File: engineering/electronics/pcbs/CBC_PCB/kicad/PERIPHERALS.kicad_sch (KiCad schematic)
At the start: 7 parts, among them J2 AT13-12PB-BM03

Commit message: electronics: integrate CBC PCB updates
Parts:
- C25, C26: symbol EasyEDA_Lib:CC0402KRX7R7BB104 -> CBC_PCB:CC0402KRX7R7BB104
- J2: symbol 2026-04-30_07-21-07:AT13-12PB-BM03 -> CBC_PCB:AT13-12PB-BM03
- R10, R11: symbol EasyEDA_Lib:RC0402FR-074K7L -> CBC_PCB:RC0402FR-074K7L
- U1, U6: symbol EasyEDA_Lib:DS18B20Z+T&amp;R -> CBC_PCB:DS18B20Z+T&amp;R

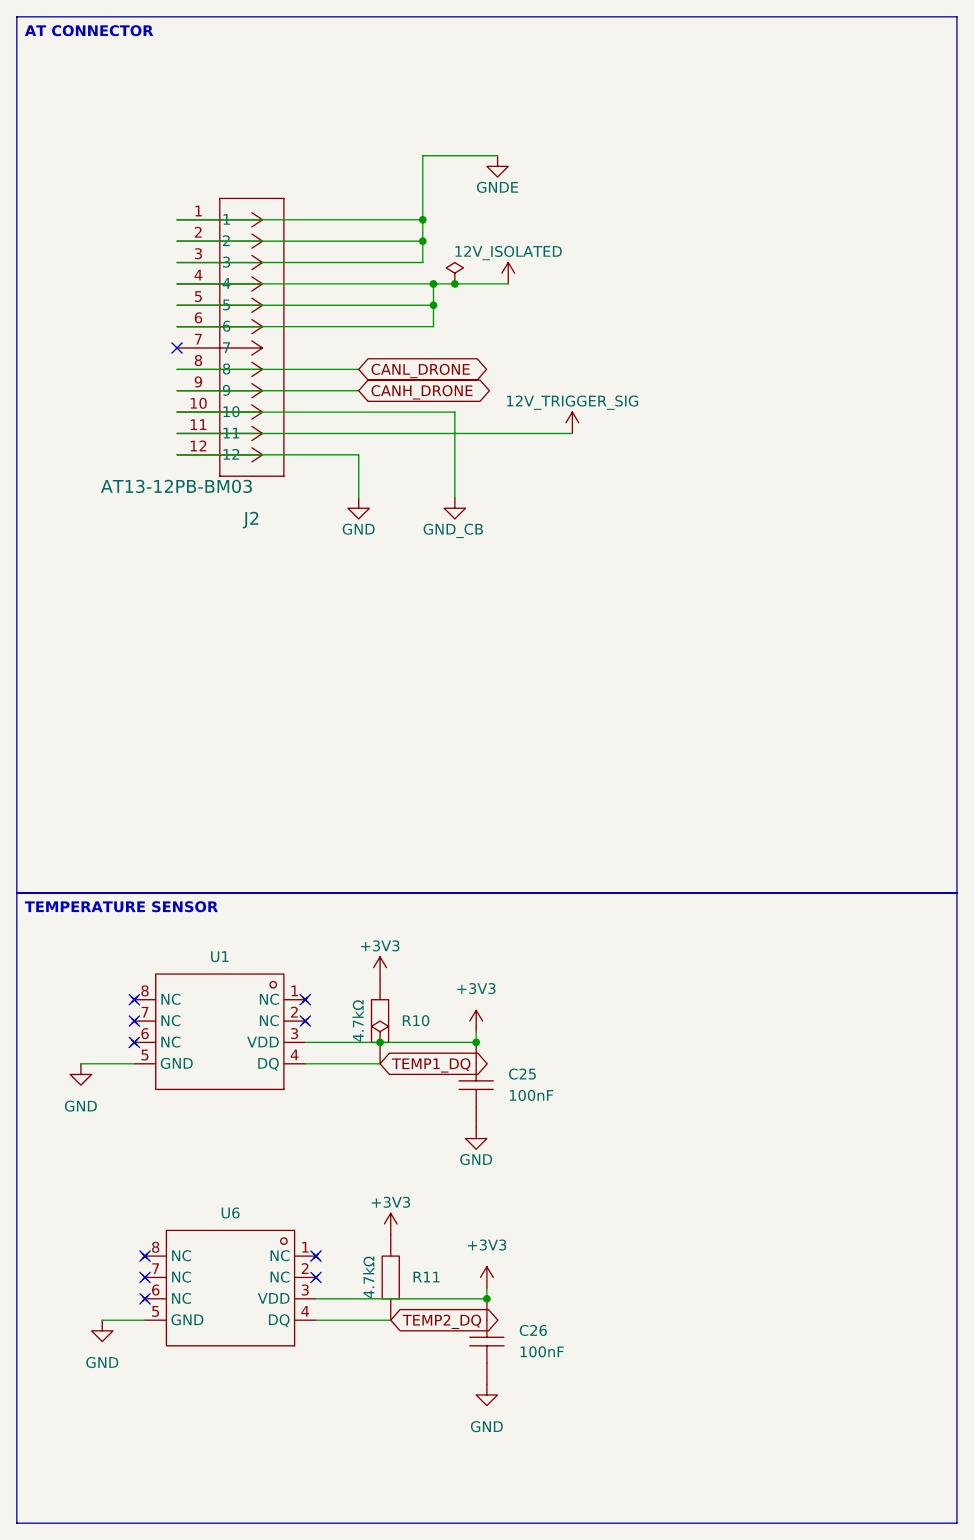
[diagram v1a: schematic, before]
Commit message: electronics: update CMAIN and CBC PCB files
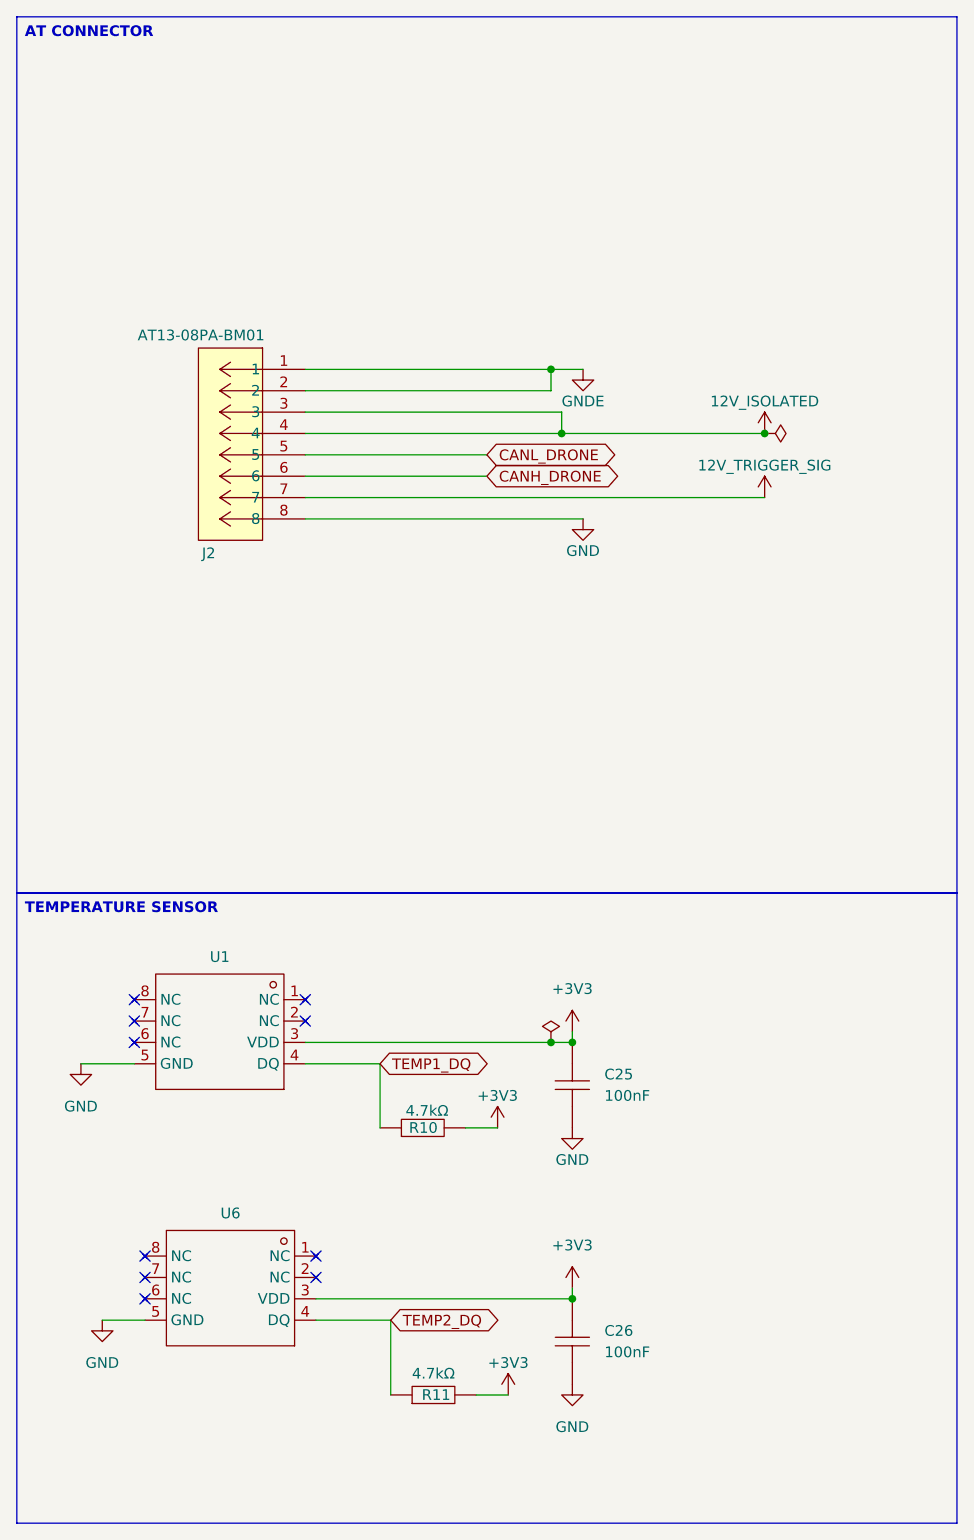
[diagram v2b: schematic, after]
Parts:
- removed J2: AT13-12PB-BM03, CBC_PCB:CONN_AT13-12X-BMXX_AMP, symbol CBC_PCB:AT13-12PB-BM03
- added J2: ${ALTIUM_VALUE}, CBC_PCB:AT13-08PA-BM01, symbol CBC_PCB:AT13-08PA-BM01
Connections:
- net 12V_ISOLATED: now also J2.3, J2.4
- net 12V_TRIGGER_SIG: now also J2.7
- net CANH_DRONE: now also J2.6
- net CANL_DRONE: now also J2.5
- net GND: now also J2.8
- net GNDE: now also J2.1, J2.2
- no-connect marks 11 -> 10
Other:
- moved on the sheet: C25, C26, R10, R11

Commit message: feat: integrate June PCB updates
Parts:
- J2: value ${ALTIUM_VALUE} -> B08B-JWPF-SK-R; footprint CBC_PCB:AT13-08PA-BM01 -> CBC_PCB:B08B-JWPF-SK-R; symbol CBC_PCB:AT13-08PA-BM01 -> CBC_PCB:B08B-JWPF-SK-R; ALTIUM_VALUE AT13-08PA-BM01 -> (none); MFR Amphenol SINE Systems -> (none); MPN AT13-08PA-BM01 -> (none); SUPPLIER Mouser -> (none); SUPPLIER PART NUMBER 654-AT13-08PA-BM01 -> (none)
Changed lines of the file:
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@@
 	)
 	(symbol
-		(lib_id "CBC_PCB:AT13-08PA-BM01")
+		(lib_id "CBC_PCB:B08B-JWPF-SK-R")
 		(at 46.99 55.88 0)
 		(mirror y)
@@
 			)
 		)
-		(property "Value" "${ALTIUM_VALUE}"
+		(property "Value" "B08B-JWPF-SK-R"
 			(at 42.164 52.578 0)
 			(show_name no)
@@
 			)
 		)
-		(property "Footprint" "CBC_PCB:AT13-08PA-BM01"
-			(at 31.496 43.688 0)
+		(property "Footprint" "CBC_PCB:B08B-JWPF-SK-R"
+			(at 32.258 43.434 0)
 			(hide yes)
 			(show_name no)
@@
 			)
 		)
-		(property "Datasheet" "AT13-08-BM01"
-			(at 39.116 46.736 0)
+		(property "Datasheet" "B08B-JWPF-SK-R"
+			(at 37.846 46.482 0)
 			(hide yes)
 			(show_name no)
@@
 			)
 		)
-		(property "Description" "Automotive Connectors RA Flng Mnt PCB Rcpt 8POS Gry Gld Cont A"
-			(at 46.99 55.88 0)
+		(property "Description" "B08B-JWPF-SK-R"
+			(at 37.592 49.022 0)
 			(hide yes)
 			(show_name no)
@@
 			)
 		)
-		(property "SUPPLIER PART NUMBER" "654-AT13-08PA-BM01"
+		(property "SUPPLIER PART NUMBER" ""
 			(at 46.99 55.88 0)
 			(hide yes)
@@
 			)
 		)
-		(property "SUPPLIER" "Mouser"
+		(property "SUPPLIER" ""
 			(at 46.99 55.88 0)
 			(hide yes)
@@
 			)
 		)
-		(property "MFR" "Amphenol SINE Systems"
+		(property "MFR" ""
 			(at 46.99 55.88 0)
 			(hide yes)
@@
 			)
 		)
-		(property "MPN" "AT13-08PA-BM01"
+		(property "MPN" ""
 			(at 46.99 55.88 0)
 			(hide yes)
@@
 			)
 		)
-		(property "ALTIUM_VALUE" "AT13-08PA-BM01"
+		(property "ALTIUM_VALUE" ""
 			(at 47.498 71.374 0)
 			(hide yes)
